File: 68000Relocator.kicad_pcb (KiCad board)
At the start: 2 copper layers, 97.4 x 97.4 mm, 3 parts, among them P99 OSHW_LOGO, U1 68000D, U2 68000D

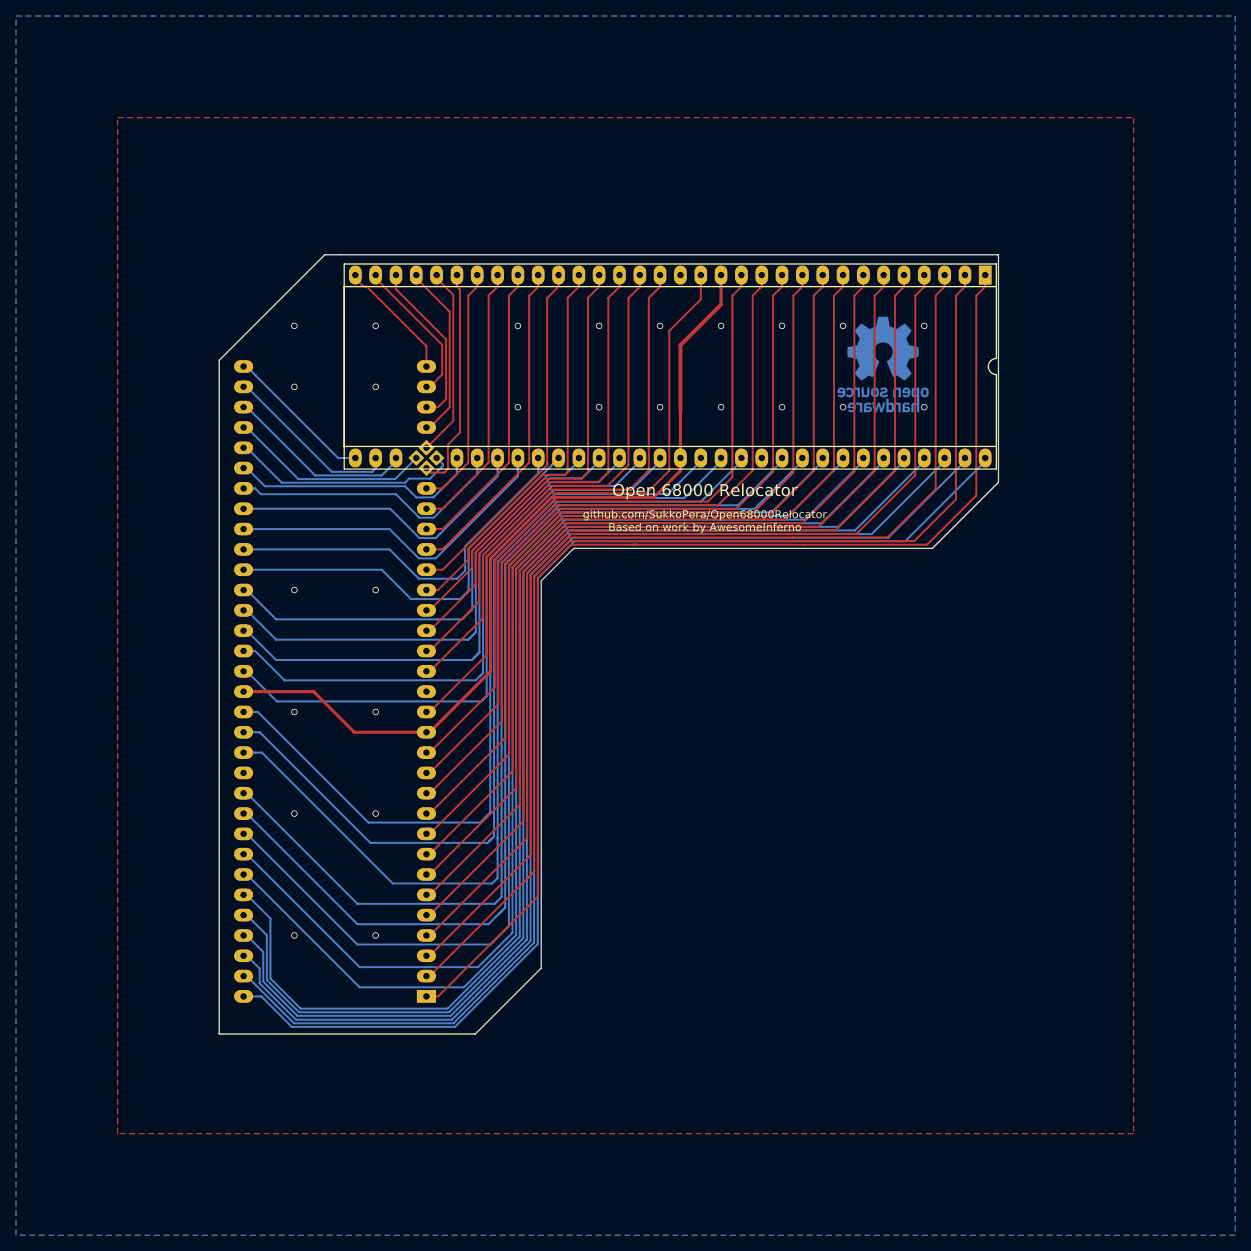
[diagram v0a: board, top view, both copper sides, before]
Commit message: Change track routing so that PCB is less tall
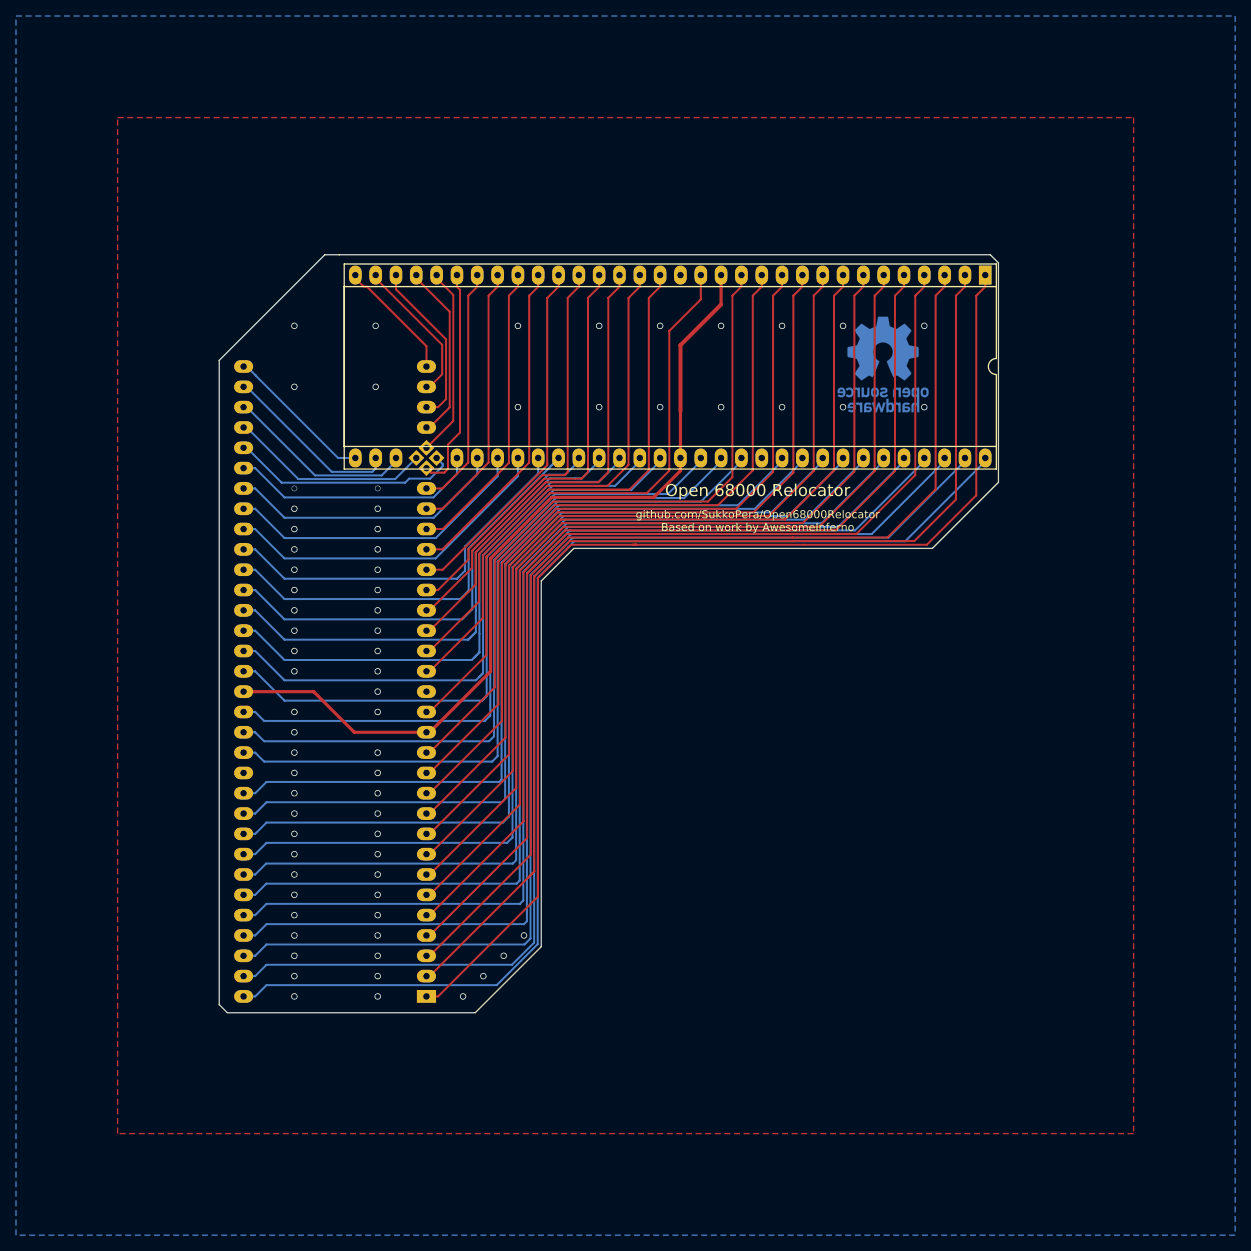
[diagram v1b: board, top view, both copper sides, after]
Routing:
- net /A23: track 114.5 -> 92.9 mm
- net /A21: track 103.8 -> 83.4 mm
- net /D14: track 126.0 -> 105.7 mm
- net /D10: track 145.9 -> 125.6 mm
- net /D15: track 120.8 -> 100.8 mm
- net /D13: track 129.9 -> 110.5 mm
- net /D12: track 134.1 -> 115.5 mm
- net /A22: track 106.4 -> 88.0 mm
- net /D11: track 138.2 -> 121.0 mm
- net /D9: track 146.6 -> 130.5 mm
- net /D8: track 147.4 -> 135.5 mm
- net /D7: track 148.6 -> 140.7 mm
- net /D6: track 149.3 -> 144.5 mm
- net /D5: track 151.2 -> 148.0 mm
- net /A15: track 51.8 -> 54.3 mm
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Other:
- board size 97.4 x 97.4 mm -> 97.4 x 94.7 mm

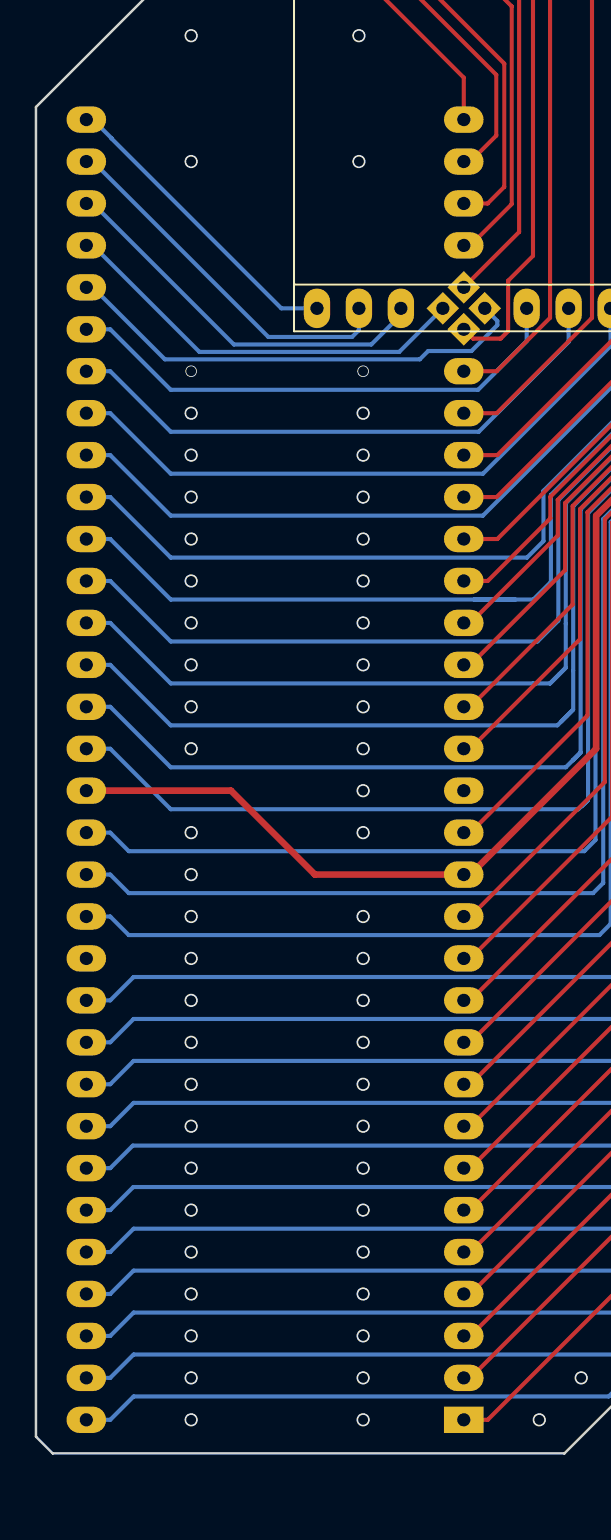
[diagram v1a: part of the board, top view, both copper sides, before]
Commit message: Add pin names on silkscreen
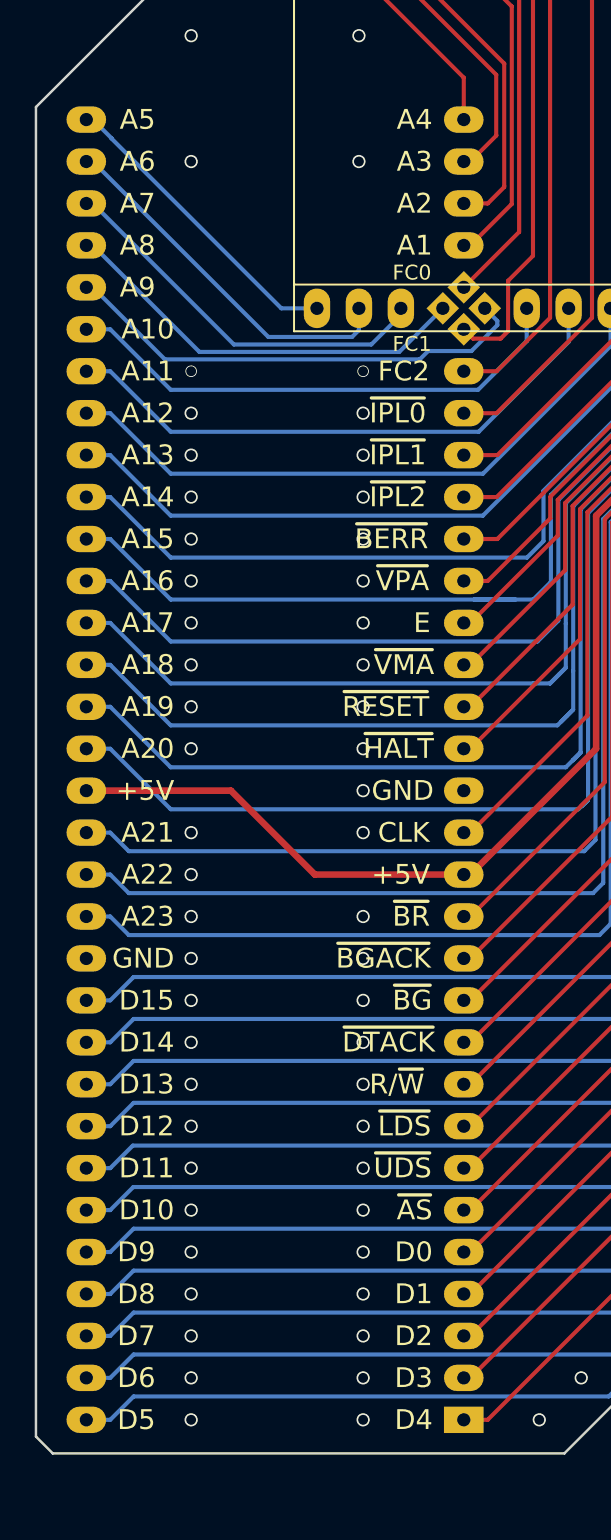
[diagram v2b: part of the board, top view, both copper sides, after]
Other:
- board text added: "+5V"
- board text added: "A1"
- board text added: "A10"
- board text added: "A11"
- board text added: "A12"
- board text added: "A13"
- board text added: "A14"
- board text added: "A15"
- board text added: "A16"
- board text added: "A17"
- board text added: "A18"
- board text added: "A19"
- board text added: "A2"
- board text added: "A20"
- board text added: "A21"
- board text added: "A22"
- board text added: "A23"
- board text added: "A3"
- board text added: "A4"
- board text added: "A5"
- board text added: "A6"
- board text added: "A7"
- board text added: "A8"
- board text added: "A9"
- board text added: "CLK"
- board text added: "D0"
- board text added: "D1"
- board text added: "D10"
- board text added: "D11"
- board text added: "D12"
- board text added: "D13"
- board text added: "D14"
- board text added: "D15"
- board text added: "D2"
- board text added: "D3"
- board text added: "D4"
- board text added: "D5"
- board text added: "D6"
- board text added: "D7"
- board text added: "D8"
- board text added: "D9"
- board text added: "E"
- board text added: "FC0"
- board text added: "FC1"
- board text added: "FC2"
- board text added: "GND"
- board text added: "R/~W"
- board text added: "~AS"
- board text added: "~BERR"
- board text added: "~BG"
- board text added: "~BGACK"
- board text added: "~BR"
- board text added: "~DTACK"
- board text added: "~HALT"
- board text added: "~IPL0"
- board text added: "~IPL1"
- board text added: "~IPL2"
- board text added: "~LDS"
- board text added: "~RESET"
- board text added: "~UDS"
- board text added: "~VMA"
- board text added: "~VPA"
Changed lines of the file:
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@@
   (general
     (thickness 1.6)
-    (drawings 20)
+    (drawings 84)
     (tracks 612)
     (zones 0)
@@
       (xy 0.633952 5.96402) (xy 0.746535 5.366828)) (layer B.Cu) (width 0.01))
   )
+  (gr_text D2 (at 110.871 134.874) (layer F.SilkS)
+    (effects (font (size 1.2 1.2) (thickness 0.2)) (justify left))
+  )
+  (gr_text ~IPL1 (at 109.347 81.534) (layer F.SilkS)
+    (effects (font (size 1.2 1.2) (thickness 0.2)) (justify left))
+  )
+  (gr_text D1 (at 110.871 132.334) (layer F.SilkS)
+    (effects (font (size 1.2 1.2) (thickness 0.2)) (justify left))
+  )
+  (gr_text GND (at 109.474 101.854) (layer F.SilkS)
+    (effects (font (size 1.2 1.2) (thickness 0.2)) (justify left))
+  )
+  (gr_text ~IPL2 (at 109.347 84.074) (layer F.SilkS)
+    (effects (font (size 1.2 1.2) (thickness 0.2)) (justify left))
+  )
+  (gr_text A1 (at 110.998 68.834) (layer F.SilkS)
+    (effects (font (size 1.2 1.2) (thickness 0.2)) (justify left))
+  )
+  (gr_text E (at 112.014 91.694) (layer F.SilkS)
+    (effects (font (size 1.2 1.2) (thickness 0.2)) (justify left))
+  )
+  (gr_text ~BERR (at 108.458 86.614) (layer F.SilkS)
+    (effects (font (size 1.2 1.2) (thickness 0.2)) (justify left))
+  )
+  (gr_text A4 (at 110.998 61.214) (layer F.SilkS)
+    (effects (font (size 1.2 1.2) (thickness 0.2)) (justify left))
+  )
+  (gr_text ~BG (at 110.744 114.554) (layer F.SilkS)
+    (effects (font (size 1.2 1.2) (thickness 0.2)) (justify left))
+  )
+  (gr_text ~BGACK (at 107.315 112.014) (layer F.SilkS)
+    (effects (font (size 1.2 1.2) (thickness 0.2)) (justify left))
+  )
+  (gr_text ~LDS (at 109.855 122.174) (layer F.SilkS)
+    (effects (font (size 1.2 1.2) (thickness 0.2)) (justify left))
+  )
+  (gr_text ~IPL0 (at 109.347 78.994) (layer F.SilkS)
+    (effects (font (size 1.2 1.2) (thickness 0.2)) (justify left))
+  )
+  (gr_text ~RESET (at 107.696 96.774) (layer F.SilkS)
+    (effects (font (size 1.2 1.2) (thickness 0.2)) (justify left))
+  )
+  (gr_text ~UDS (at 109.601 124.714) (layer F.SilkS)
+    (effects (font (size 1.2 1.2) (thickness 0.2)) (justify left))
+  )
+  (gr_text ~VPA (at 109.728 89.154) (layer F.SilkS)
+    (effects (font (size 1.2 1.2) (thickness 0.2)) (justify left))
+  )
+  (gr_text R/~W (at 109.347 119.634) (layer F.SilkS)
+    (effects (font (size 1.2 1.2) (thickness 0.2)) (justify left))
+  )
+  (gr_text +5V (at 109.474 106.934) (layer F.SilkS)
+    (effects (font (size 1.2 1.2) (thickness 0.2)) (justify left))
+  )
+  (gr_text CLK (at 109.855 104.394) (layer F.SilkS)
+    (effects (font (size 1.2 1.2) (thickness 0.2)) (justify left))
+  )
+  (gr_text D3 (at 110.871 137.414) (layer F.SilkS)
+    (effects (font (size 1.2 1.2) (thickness 0.2)) (justify left))
+  )
+  (gr_text ~VMA (at 109.601 94.234) (layer F.SilkS)
+    (effects (font (size 1.2 1.2) (thickness 0.2)) (justify left))
+  )
+  (gr_text ~HALT (at 108.966 99.314) (layer F.SilkS)
+    (effects (font (size 1.2 1.2) (thickness 0.2)) (justify left))
+  )
+  (gr_text ~BR (at 110.744 109.474) (layer F.SilkS)
+    (effects (font (size 1.2 1.2) (thickness 0.2)) (justify left))
+  )
+  (gr_text A3 (at 110.998 63.754) (layer F.SilkS)
+    (effects (font (size 1.2 1.2) (thickness 0.2)) (justify left))
+  )
+  (gr_text FC0 (at 110.744 70.485) (layer F.SilkS)
+    (effects (font (size 0.9 0.9) (thickness 0.15)) (justify left))
+  )
+  (gr_text D0 (at 110.871 129.794) (layer F.SilkS)
+    (effects (font (size 1.2 1.2) (thickness 0.2)) (justify left))
+  )
+  (gr_text A2 (at 110.998 66.294) (layer F.SilkS)
+    (effects (font (size 1.2 1.2) (thickness 0.2)) (justify left))
+  )
+  (gr_text ~DTACK (at 107.696 117.094) (layer F.SilkS)
+    (effects (font (size 1.2 1.2) (thickness 0.2)) (justify left))
+  )
+  (gr_text FC1 (at 110.744 74.803) (layer F.SilkS)
+    (effects (font (size 0.9 0.9) (thickness 0.15)) (justify left))
+  )
+  (gr_text ~AS (at 110.998 127.254) (layer F.SilkS)
+    (effects (font (size 1.2 1.2) (thickness 0.2)) (justify left))
+  )
+  (gr_text D4 (at 110.871 139.954) (layer F.SilkS)
+    (effects (font (size 1.2 1.2) (thickness 0.2)) (justify left))
+  )
+  (gr_text FC2 (at 109.855 76.454) (layer F.SilkS)
+    (effects (font (size 1.2 1.2) (thickness 0.2)) (justify left))
+  )
+  (gr_text D5 (at 96.393 139.954) (layer F.SilkS)
+    (effects (font (size 1.2 1.2) (thickness 0.2)) (justify right))
+  )
+  (gr_text D6 (at 96.393 137.414) (layer F.SilkS)
+    (effects (font (size 1.2 1.2) (thickness 0.2)) (justify right))
+  )
+  (gr_text D7 (at 96.393 134.874) (layer F.SilkS)
+    (effects (font (size 1.2 1.2) (thickness 0.2)) (justify right))
+  )
+  (gr_text D8 (at 96.393 132.334) (layer F.SilkS)
+    (effects (font (size 1.2 1.2) (thickness 0.2)) (justify right))
+  )
+  (gr_text D9 (at 96.393 129.794) (layer F.SilkS)
+    (effects (font (size 1.2 1.2) (thickness 0.2)) (justify right))
+  )
+  (gr_text D10 (at 97.536 127.254) (layer F.SilkS)
+    (effects (font (size 1.2 1.2) (thickness 0.2)) (justify right))
+  )
+  (gr_text D11 (at 97.536 124.714) (layer F.SilkS)
+    (effects (font (size 1.2 1.2) (thickness 0.2)) (justify right))
+  )
+  (gr_text D12 (at 97.536 122.174) (layer F.SilkS)
+    (effects (font (size 1.2 1.2) (thickness 0.2)) (justify right))
+  )
+  (gr_text D13 (at 97.536 119.634) (layer F.SilkS)
+    (effects (font (size 1.2 1.2) (thickness 0.2)) (justify right))
+  )
+  (gr_text D14 (at 97.536 117.094) (layer F.SilkS)
+    (effects (font (size 1.2 1.2) (thickness 0.2)) (justify right))
+  )
+  (gr_text D15 (at 97.536 114.554) (layer F.SilkS)
+    (effects (font (size 1.2 1.2) (thickness 0.2)) (justify right))
+  )
+  (gr_text GND (at 97.536 112.014) (layer F.SilkS)
+    (effects (font (size 1.2 1.2) (thickness 0.2)) (justify right))
+  )
+  (gr_text A23 (at 97.536 109.474) (layer F.SilkS)
+    (effects (font (size 1.2 1.2) (thickness 0.2)) (justify right))
+  )
+  (gr_text A22 (at 97.536 106.934) (layer F.SilkS)
+    (effects (font (size 1.2 1.2) (thickness 0.2)) (justify right))
+  )
+  (gr_text A21 (at 97.536 104.394) (layer F.SilkS)
+    (effects (font (size 1.2 1.2) (thickness 0.2)) (justify right))
+  )
+  (gr_text +5V (at 97.536 101.854) (layer F.SilkS)
+    (effects (font (size 1.2 1.2) (thickness 0.2)) (justify right))
+  )
+  (gr_text A20 (at 97.536 99.314) (layer F.SilkS)
+    (effects (font (size 1.2 1.2) (thickness 0.2)) (justify right))
+  )
+  (gr_text A19 (at 97.536 96.774) (layer F.SilkS)
+    (effects (font (size 1.2 1.2) (thickness 0.2)) (justify right))
+  )
+  (gr_text A18 (at 97.536 94.234) (layer F.SilkS)
+    (effects (font (size 1.2 1.2) (thickness 0.2)) (justify right))
+  )
+  (gr_text A17 (at 97.536 91.694) (layer F.SilkS)
+    (effects (font (size 1.2 1.2) (thickness 0.2)) (justify right))
+  )
+  (gr_text A16 (at 97.536 89.154) (layer F.SilkS)
+    (effects (font (size 1.2 1.2) (thickness 0.2)) (justify right))
+  )
+  (gr_text A15 (at 97.536 86.614) (layer F.SilkS)
+    (effects (font (size 1.2 1.2) (thickness 0.2)) (justify right))
+  )
+  (gr_text A14 (at 97.536 84.074) (layer F.SilkS)
+    (effects (font (size 1.2 1.2) (thickness 0.2)) (justify right))
+  )
+  (gr_text A13 (at 97.536 81.534) (layer F.SilkS)
+    (effects (font (size 1.2 1.2) (thickness 0.2)) (justify right))
+  )
+  (gr_text A12 (at 97.536 78.994) (layer F.SilkS)
+    (effects (font (size 1.2 1.2) (thickness 0.2)) (justify right))
+  )
+  (gr_text A11 (at 97.536 76.454) (layer F.SilkS)
+    (effects (font (size 1.2 1.2) (thickness 0.2)) (justify right))
+  )
+  (gr_text A10 (at 97.536 73.914) (layer F.SilkS)
+    (effects (font (size 1.2 1.2) (thickness 0.2)) (justify right))
+  )
+  (gr_text A9 (at 96.393 71.374) (layer F.SilkS)
+    (effects (font (size 1.2 1.2) (thickness 0.2)) (justify right))
+  )
+  (gr_text A8 (at 96.393 68.834) (layer F.SilkS)
+    (effects (font (size 1.2 1.2) (thickness 0.2)) (justify right))
+  )
+  (gr_text A7 (at 96.393 66.294) (layer F.SilkS)
+    (effects (font (size 1.2 1.2) (thickness 0.2)) (justify right))
+  )
+  (gr_text A6 (at 96.393 63.754) (layer F.SilkS)
+    (effects (font (size 1.2 1.2) (thickness 0.2)) (justify right))
+  )
+  (gr_text A5 (at 96.393 61.214) (layer F.SilkS)
+    (effects (font (size 1.2 1.2) (thickness 0.2)) (justify right))
+  )
   (gr_line (start 185.547 47.244) (end 186.563 48.26) (layer Edge.Cuts) (width 0.15))
